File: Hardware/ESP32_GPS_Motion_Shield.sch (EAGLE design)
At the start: 38 parts, among them J2 MICRO-SD_CARD_SOCKET, J7 BM06B-SRSS-TB, Q1 4.3A/20V/54mΩ, Q2 4.3A/20V/54mΩ, U1 LSM9DS1

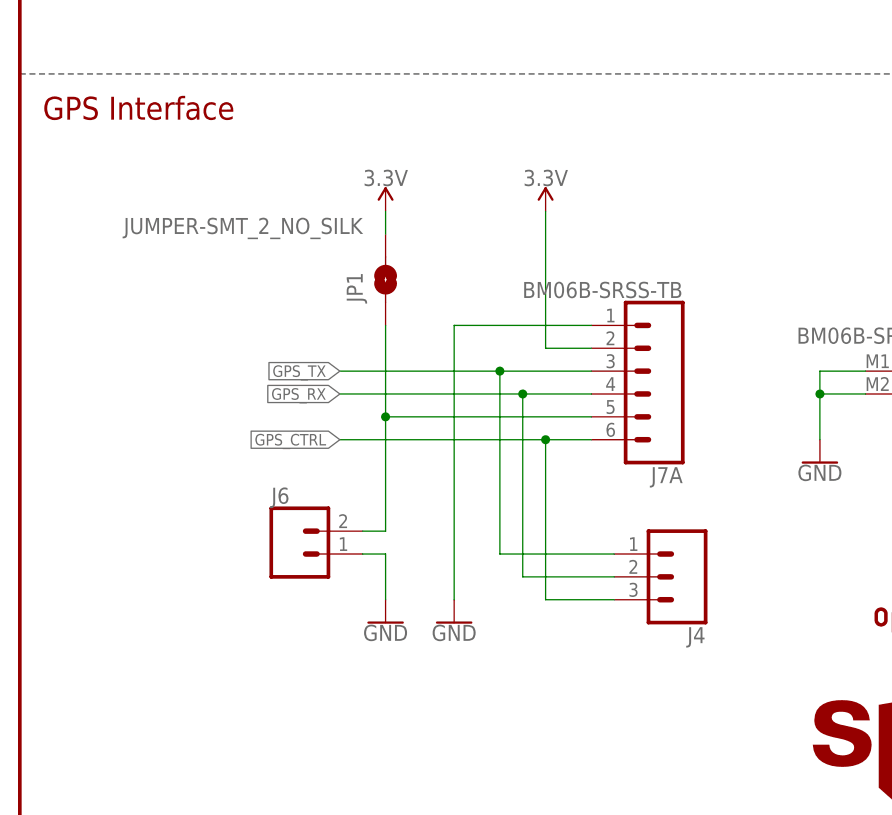
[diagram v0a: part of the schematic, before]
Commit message: Switched to other GPS jack
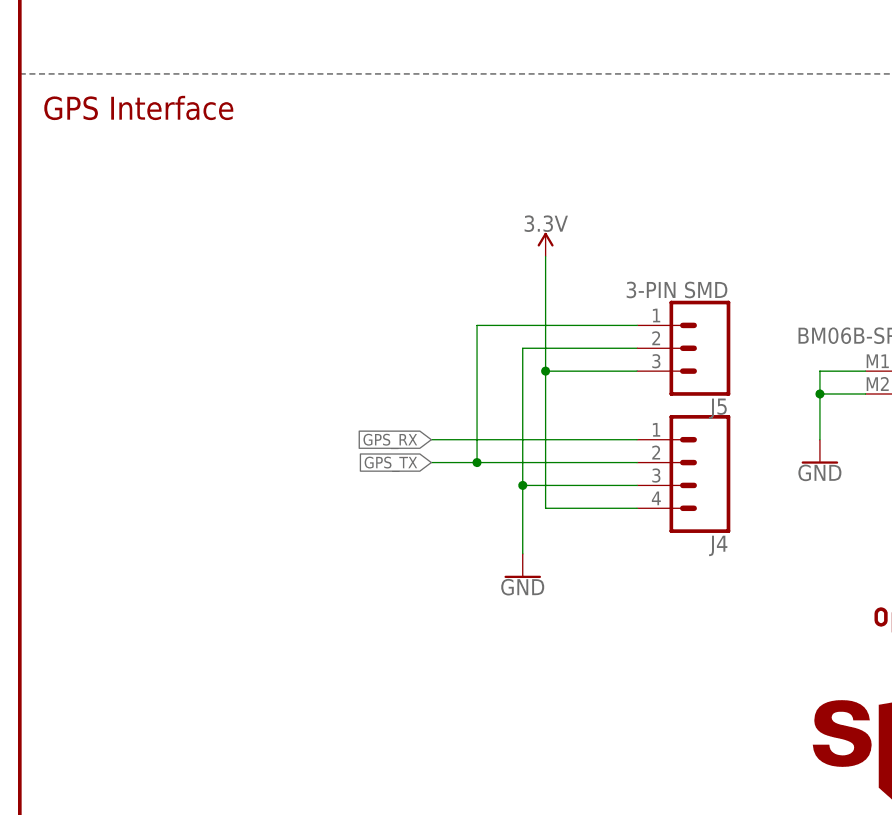
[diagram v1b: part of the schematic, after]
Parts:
- removed J6: (no value), SparkFun-Connectors:CONN_02
- removed JP1: JUMPER-SMT_2_NO_SILK, SparkFun-Jumpers:JUMPER-SMT_2_NO_SILK
- added J5: 3-PIN SMD, SparkFun-Connectors:CONN_03JST-SMD
- J4: device SparkFun-Connectors:CONN_03 -> SparkFun-Connectors:CONN_04
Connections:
- removed net N$2: J6.2, J7A.5, JP1.1
- net 3.3V: now also J4.4, J5.3; no longer J7A.2, JP1.2
- net GND: now also J4.3, J5.2; no longer J6.1, J7A.1
- net GPS_CTRL: no longer J4.3, J7A.6
- net GPS_RX: now also J4.1; no longer J4.2, J7A.4
- net GPS_TX: now also J4.2, J5.1; no longer J4.1, J7A.3
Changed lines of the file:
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@@
 <part name="B1" library="SparkFun-Boards" deviceset="ESP32_THING" device="_WO_ANT_KEEPOUT"/>
 <part name="J2" library="SparkFun-Connectors" deviceset="MICRO-SD_CARD_SOCKET" device=""/>
-<part name="JP1" library="SparkFun-Jumpers" deviceset="JUMPER-SMT_2_NO" device="_SILK"/>
 <part name="J1" library="SparkFun-Connectors" deviceset="CONN_20" device="NOSILK"/>
 <part name="J3" library="SparkFun-Connectors" deviceset="CONN_20" device="NOSILK"/>
@@
 <part name="R7" library="SparkFun-Resistors" deviceset="100KOHM" device="-0402-1/16W-1%" value="100K"/>
 <part name="R8" library="SparkFun-Resistors" deviceset="100KOHM" device="-0402-1/16W-1%" value="100K"/>
-<part name="J6" library="SparkFun-Connectors" deviceset="CONN_02" device=""/>
-<part name="J4" library="SparkFun-Connectors" deviceset="CONN_03" device=""/>
 <part name="J7" library="SparkFun-Connectors" deviceset="JST_6_PIN_HORIZONTAL" device="" value="BM06B-SRSS-TB"/>
 <part name="GND15" library="SparkFun-PowerSymbols" deviceset="GND" device=""/>
-<part name="SUPPLY7" library="SparkFun-PowerSymbols" deviceset="3.3V" device=""/>
 <part name="SUPPLY8" library="SparkFun-PowerSymbols" deviceset="3.3V" device=""/>
 <part name="SUPPLY2" library="SparkFun-PowerSymbols" deviceset="3.3V" device=""/>
 <part name="SUPPLY6" library="SparkFun-PowerSymbols" deviceset="3.3V" device=""/>
 <part name="R1" library="SparkFun-Resistors" deviceset="470OHM" device="-0603-1/10W-1%" value="470"/>
-<part name="GND2" library="SparkFun-PowerSymbols" deviceset="GND" device=""/>
 <part name="GND3" library="SparkFun-PowerSymbols" deviceset="GND" device=""/>
 <part name="GND4" library="SparkFun-PowerSymbols" deviceset="GND" device=""/>
@@
 <part name="TP4" library="SparkFun-Connectors" deviceset="TEST-POINT" device="3"/>
 <part name="TP5" library="SparkFun-Connectors" deviceset="TEST-POINT" device="3"/>
+<part name="J5" library="SparkFun-Connectors" deviceset="CONN_03" device="JST-SMD" value="3-PIN SMD"/>
+<part name="J4" library="SparkFun-Connectors" deviceset="CONN_04" device=""/>
 </parts>
 <sheets>
@@
 <instance part="B1" gate="G$1" x="198.12" y="76.2"/>
 <instance part="J2" gate="1" x="182.88" y="152.4"/>
-<instance part="JP1" gate="G$1" x="40.64" y="60.96" smashed="yes" rot="R90">
-<attribute name="NAME" x="38.1" y="58.42" size="1.778" layer="95" font="vector" rot="R90"/>
-<attribute name="VALUE" x="38.1" y="66.04" size="1.778" layer="96" font="vector" rot="R180" align="top-left"/>
-</instance>
 <instance part="J1" gate="G$1" x="154.94" y="48.26"/>
 <instance part="J3" gate="G$1" x="241.3" y="106.68" rot="R180"/>
@@
 <instance part="R7" gate="G$1" x="218.44" y="152.4"/>
 <instance part="R8" gate="G$1" x="208.28" y="147.32"/>
-<instance part="J6" gate="G$1" x="30.48" y="30.48"/>
-<instance part="J4" gate="J$1" x="73.66" y="27.94" rot="R180"/>
-<instance part="J7" gate="A" x="68.58" y="50.8" rot="R180"/>
 <instance part="J7" gate="B" x="101.6" y="50.8" rot="R180"/>
 <instance part="GND15" gate="1" x="88.9" y="40.64"/>
-<instance part="SUPPLY7" gate="G$1" x="40.64" y="68.58"/>
-<instance part="SUPPLY8" gate="G$1" x="58.42" y="68.58"/>
+<instance part="SUPPLY8" gate="G$1" x="58.42" y="63.5"/>
 <instance part="SUPPLY2" gate="G$1" x="162.56" y="165.1"/>
 <instance part="SUPPLY6" gate="G$1" x="231.14" y="165.1"/>
 <instance part="R1" gate="G$1" x="119.38" y="66.04" rot="R180"/>
-<instance part="GND2" gate="1" x="40.64" y="22.86"/>
-<instance part="GND3" gate="1" x="48.26" y="22.86"/>
+<instance part="GND3" gate="1" x="55.88" y="27.94"/>
 <instance part="GND4" gate="1" x="127" y="50.8"/>
 <instance part="GND5" gate="1" x="185.42" y="129.54"/>
@@
 <instance part="TP4" gate="G$1" x="116.84" y="106.68"/>
 <instance part="TP5" gate="G$1" x="116.84" y="104.14"/>
+<instance part="J5" gate="J$1" x="76.2" y="53.34" rot="R180"/>
+<instance part="J4" gate="G$1" x="73.66" y="40.64" rot="R180"/>
 </instances>
 <busses>
@@
 </segment>
 <segment>
-<pinref part="JP1" gate="G$1" pin="2"/>
-<pinref part="SUPPLY7" gate="G$1" pin="3.3V"/>
-<wire x1="40.64" y1="68.58" x2="40.64" y2="66.04" width="0.1524" layer="91"/>
-</segment>
-<segment>
-<wire x1="58.42" y1="68.58" x2="58.42" y2="53.34" width="0.1524" layer="91"/>
+<wire x1="58.42" y1="63.5" x2="58.42" y2="50.8" width="0.1524" layer="91"/>
 <pinref part="SUPPLY8" gate="G$1" pin="3.3V"/>
-<wire x1="63.5" y1="53.34" x2="58.42" y2="53.34" width="0.1524" layer="91"/>
-<pinref part="J7" gate="A" pin="2"/>
+<wire x1="68.58" y1="50.8" x2="58.42" y2="50.8" width="0.1524" layer="91"/>
+<pinref part="J5" gate="J$1" pin="3"/>
+<wire x1="58.42" y1="50.8" x2="58.42" y2="35.56" width="0.1524" layer="91"/>
+<pinref part="J4" gate="G$1" pin="4"/>
+<wire x1="58.42" y1="35.56" x2="68.58" y2="35.56" width="0.1524" layer="91"/>
+<junction x="58.42" y="50.8"/>
 </segment>
 <segment>
@@
 </segment>
 <segment>
-<pinref part="J6" gate="G$1" pin="1"/>
-<wire x1="38.1" y1="30.48" x2="40.64" y2="30.48" width="0.1524" layer="91"/>
-<wire x1="40.64" y1="30.48" x2="40.64" y2="25.4" width="0.1524" layer="91"/>
-<pinref part="GND2" gate="1" pin="GND"/>
-</segment>
-<segment>
-<wire x1="63.5" y1="55.88" x2="48.26" y2="55.88" width="0.1524" layer="91"/>
-<wire x1="48.26" y1="55.88" x2="48.26" y2="25.4" width="0.1524" layer="91"/>
-<pinref part="J7" gate="A" pin="1"/>
+<wire x1="68.58" y1="53.34" x2="55.88" y2="53.34" width="0.1524" layer="91"/>
+<wire x1="55.88" y1="53.34" x2="55.88" y2="38.1" width="0.1524" layer="91"/>
 <pinref part="GND3" gate="1" pin="GND"/>
+<pinref part="J5" gate="J$1" pin="2"/>
+<pinref part="J4" gate="G$1" pin="3"/>
+<wire x1="55.88" y1="38.1" x2="55.88" y2="30.48" width="0.1524" layer="91"/>
+<wire x1="68.58" y1="38.1" x2="55.88" y2="38.1" width="0.1524" layer="91"/>
+<junction x="55.88" y="38.1"/>
 </segment>
 <segment>
@@
 <net name="GPS_RX" class="0">
 <segment>
-<wire x1="63.5" y1="48.26" x2="55.88" y2="48.26" width="0.1524" layer="91"/>
-<wire x1="66.04" y1="27.94" x2="55.88" y2="27.94" width="0.1524" layer="91"/>
-<wire x1="55.88" y1="27.94" x2="55.88" y2="48.26" width="0.1524" layer="91"/>
-<wire x1="55.88" y1="48.26" x2="35.56" y2="48.26" width="0.1524" layer="91"/>
-<junction x="55.88" y="48.26"/>
-<pinref part="J4" gate="J$1" pin="2"/>
-<pinref part="J7" gate="A" pin="4"/>
-<label x="35.56" y="48.26" size="1.27" layer="95" font="vector" rot="R180" xref="yes"/>
+<label x="45.72" y="43.18" size="1.27" layer="95" font="vector" rot="R180" xref="yes"/>
+<pinref part="J4" gate="G$1" pin="1"/>
+<wire x1="68.58" y1="43.18" x2="45.72" y2="43.18" width="0.1524" layer="91"/>
 </segment>
 <segment>
@@
 <net name="GPS_TX" class="0">
 <segment>
-<wire x1="63.5" y1="50.8" x2="53.34" y2="50.8" width="0.1524" layer="91"/>
-<wire x1="66.04" y1="30.48" x2="53.34" y2="30.48" width="0.1524" layer="91"/>
-<wire x1="53.34" y1="30.48" x2="53.34" y2="50.8" width="0.1524" layer="91"/>
-<wire x1="53.34" y1="50.8" x2="35.56" y2="50.8" width="0.1524" layer="91"/>
-<junction x="53.34" y="50.8"/>
-<pinref part="J4" gate="J$1" pin="1"/>
-<pinref part="J7" gate="A" pin="3"/>
-<label x="35.56" y="50.8" size="1.27" layer="95" font="vector" rot="R180" xref="yes"/>
+<wire x1="68.58" y1="55.88" x2="50.8" y2="55.88" width="0.1524" layer="91"/>
+<wire x1="50.8" y1="55.88" x2="50.8" y2="40.64" width="0.1524" layer="91"/>
+<wire x1="50.8" y1="40.64" x2="45.72" y2="40.64" width="0.1524" layer="91"/>
+<label x="45.72" y="40.64" size="1.27" layer="95" font="vector" rot="R180" xref="yes"/>
+<pinref part="J5" gate="J$1" pin="1"/>
+<pinref part="J4" gate="G$1" pin="2"/>
+<wire x1="68.58" y1="40.64" x2="50.8" y2="40.64" width="0.1524" layer="91"/>
+<junction x="50.8" y="40.64"/>
 </segment>
 <segment>
@@
 <net name="GPS_CTRL" class="0">
 <segment>
-<wire x1="63.5" y1="43.18" x2="58.42" y2="43.18" width="0.1524" layer="91"/>
-<wire x1="58.42" y1="43.18" x2="58.42" y2="25.4" width="0.1524" layer="91"/>
-<wire x1="58.42" y1="25.4" x2="66.04" y2="25.4" width="0.1524" layer="91"/>
-<wire x1="58.42" y1="43.18" x2="35.56" y2="43.18" width="0.1524" layer="91"/>
-<junction x="58.42" y="43.18"/>
-<pinref part="J4" gate="J$1" pin="3"/>
-<pinref part="J7" gate="A" pin="6"/>
-<label x="35.56" y="43.18" size="1.27" layer="95" font="vector" rot="R180" xref="yes"/>
-</segment>
-<segment>
 <pinref part="J1" gate="G$1" pin="18"/>
 <pinref part="B1" gate="G$1" pin="38"/>
@@
 </segment>
 </net>
-<net name="N$2" class="0">
-<segment>
-<wire x1="63.5" y1="45.72" x2="40.64" y2="45.72" width="0.1524" layer="91"/>
-<pinref part="JP1" gate="G$1" pin="1"/>
-<wire x1="40.64" y1="55.88" x2="40.64" y2="45.72" width="0.1524" layer="91"/>
-<pinref part="J6" gate="G$1" pin="2"/>
-<wire x1="38.1" y1="33.02" x2="40.64" y2="33.02" width="0.1524" layer="91"/>
-<wire x1="40.64" y1="33.02" x2="40.64" y2="45.72" width="0.1524" layer="91"/>
-<junction x="40.64" y="45.72"/>
-<pinref part="J7" gate="A" pin="5"/>
-</segment>
-</net>

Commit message: Ready for review
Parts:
- removed J5: 3-PIN SMD, SparkFun-Connectors:CONN_03JST-SMD
- removed J7: BM06B-SRSS-TB, SparkFun-Connectors:JST_6_PIN_HORIZONTAL
- added FD3, FD4: FIDUCIALUFIDUCIAL, SparkFun-Aesthetics:FIDUCIALUFIDUCIAL
- added J6: 3-PIN SMD, SparkFun-Connectors:CONN_03JST-SMD
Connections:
- net 3.3V: now also J6.1; no longer J5.3
- net GND: now also J6.2; no longer J5.2, J7B.1, J7B.2
- net GPS_TX: now also J6.3; no longer J5.1
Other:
- note added: "Mag at addr: 0x1E Accel/Gyro at addr: 0x6B"
- note added: "Use 3 pin JST for GP-20U7 (SFE PN GPS-13740), or wire to 4 pin 0.1 inch header"
- note added: "User controlled from GPIO 37"
- note added: "v01"
- note removed: "v10"
- moved on the sheet: D1, J4, R1

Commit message: Ready for QC review
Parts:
- removed LOGO4: SFE_LOGO_NAME.1_INCH, SparkFun-Aesthetics:SFE_LOGO_NAME.1_INCH
- removed R8: 100K, SparkFun-Resistors:100KOHM-0402-1/16W-1%
- added LOGO2: SFE_LOGO_NAME_FLAME.2_INCH, SparkFun-Aesthetics:SFE_LOGO_NAME_FLAME.2_INCH
- added R2, R4, R5, R6: 10k, SparkFun-Resistors:10KOHM-0603-1/10W-1%
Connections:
- removed net GPS_CTRL: B1.38, J1.18
- removed net N$11: J2.CD1, R8.1
- new net 3.3V_B: B1.3V3@5, J1.5
- new net SD_CD: B1.38, J1.18, J2.CD2
- new net VUSB_B: B1.VUSB@2, J1.2
- new net V_BATT_B: B1.VBAT@3, J1.3
- net 3.3V: now also R2.2, R4.2, R5.2, R6.2; no longer B1.3V3@5, J1.5, R8.2
- net GND: now also J2.CD1
- net SD_CS: now also R2.1
- net SD_DO: now also R4.1
- net VDDIO_CTRL: now also R5.1
- net VDD_CTRL: now also R6.1
- net VUSB: no longer B1.VUSB@2, J1.2
- net V_BATT: no longer B1.VBAT@3, J1.3
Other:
- moved on the sheet: C8, D1, J2, R1, R3, R7
